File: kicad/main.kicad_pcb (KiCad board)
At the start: 2 copper layers, 13 parts, among them J1 Conn_02x14_Counter_Clockwise, U1 7421, U2 74LS86, U3 74LS138, U4 7421, U5 7421, U6 74LS138

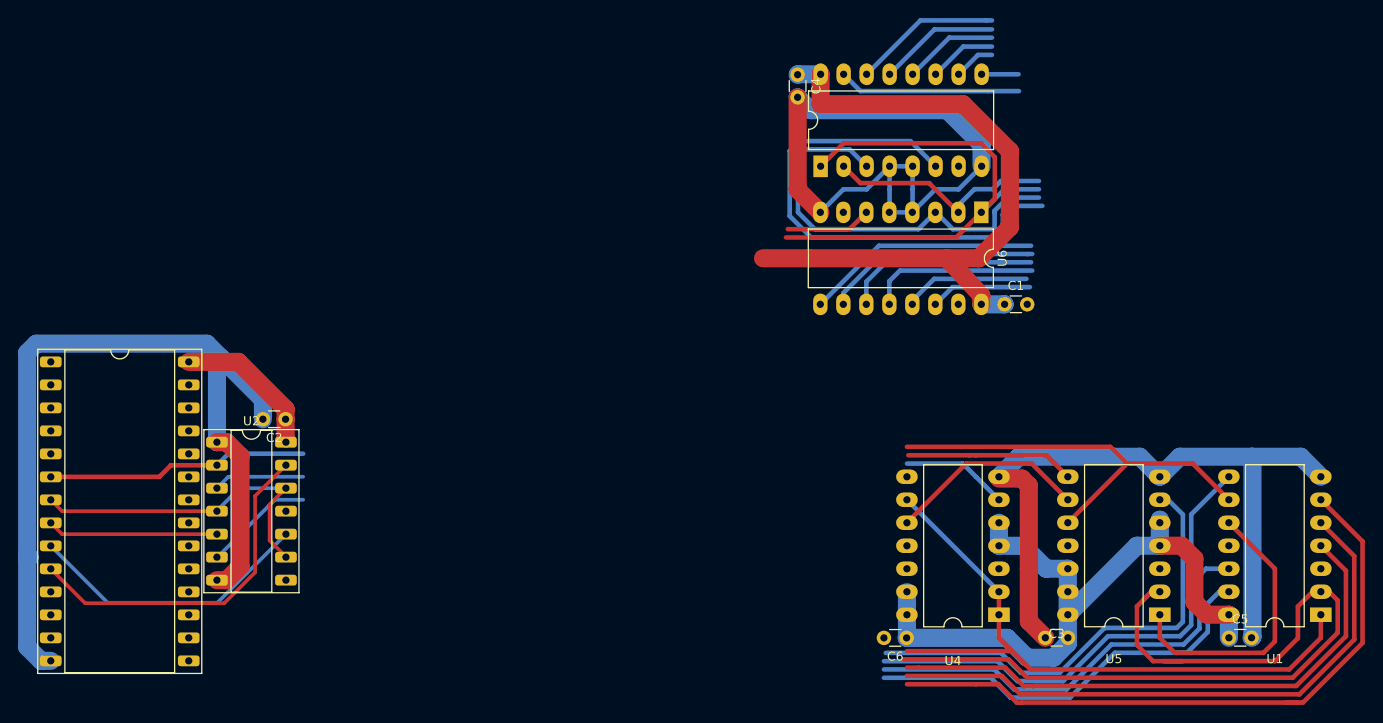
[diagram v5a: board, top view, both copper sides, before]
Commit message: finished single dmux
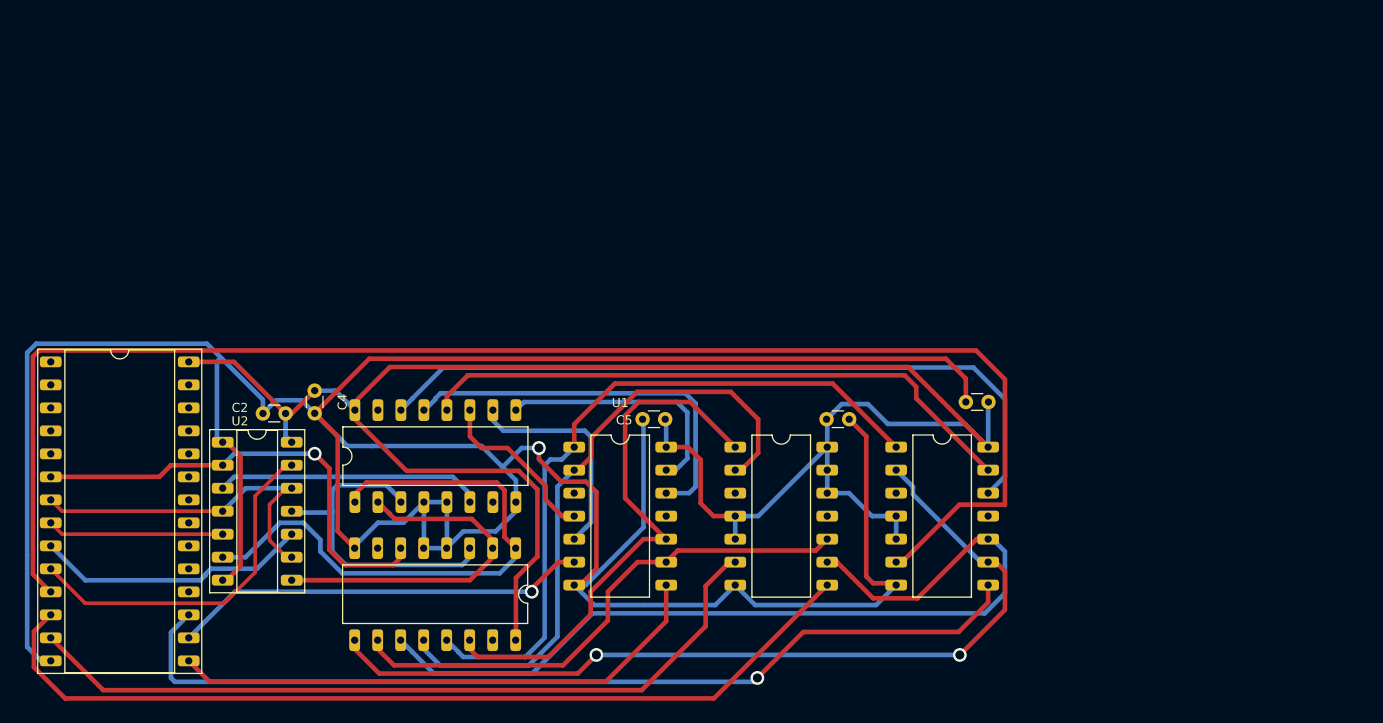
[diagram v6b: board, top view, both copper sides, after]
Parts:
- removed C1: 100n, Capacitor_THT:C_Disc_D3.0mm_W1.6mm_P2.50mm
- moved U1 84.5 mm to (108.0, 71.7), turned to 0 degrees
- moved C5 66.8 mm to (118.1, 68.6), turned to 180 degrees
- moved C4 63.7 mm to (79.4, 65.4)
- moved U3 63.4 mm to (83.8, 77.7)
- moved U6 63.4 mm to (101.6, 82.8)
- moved U5 50.4 mm to (125.8, 71.7), turned to 0 degrees
- moved C3 36.0 mm to (135.9, 68.6), turned to 0 degrees
- moved C6 27.6 mm to (153.8, 66.7)
- moved U4 21.7 mm to (143.6, 71.7), turned to 0 degrees
- moved U2 0.64 mm to (69.2, 71.1)
- moved C2 0.64 mm to (76.2, 67.9)
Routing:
- net /B_H_OUT: track 11.8 -> 164.2 mm
- net GND: track 249.3 -> 367.8 mm, vias 0 -> 1
- net /Y_L_OUT: track 0.00 -> 103.8 mm, vias 0 -> 1
- net /G_H_OUT: track 18.6 -> 100.8 mm
- net Net-(U3-~{Y1}): track 16.3 -> 81.3 mm
- net Net-(U6-~{Y6}): track 40.3 -> 98.2 mm, vias 0 -> 2
- net Net-(U6-~{Y4}): track 43.7 -> 101.1 mm
- net Net-(U3-~{Y3}): track 10.4 -> 67.3 mm
- net Net-(U3-~{Y4}): track 70.2 -> 19.0 mm
- net +5V: track 170.0 -> 220.8 mm
- net Net-(U3-~{Y5}): track 71.8 -> 24.8 mm
- net Net-(U6-~{Y3}): track 112.7 -> 71.3 mm
- net /adressInverter//PWM: track 66.5 -> 29.5 mm
- net /Y_H_OUT: track 51.2 -> 86.5 mm
- net /G_L_OUT: track 72.9 -> 46.2 mm, vias 0 -> 1
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
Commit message: final design
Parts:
- moved U6 2.18 mm to (101.6, 80.6)
- moved U3 1.53 mm to (83.8, 76.2)
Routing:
- net GND: track 367.8 -> 351.2 mm
- net /adressInverter/H1_OUT: track 64.0 -> 54.3 mm
- net Net-(U6-~{Y2}): track 78.5 -> 73.1 mm
- net /adressInverter/H2_OUT: track 40.4 -> 44.1 mm
- net /adressInverter/H3_OUT: track 37.4 -> 40.5 mm
- net Net-(U6-~{Y5}): track 59.0 -> 56.1 mm
- net Net-(U3-~{Y2}): track 44.0 -> 46.6 mm
- net Net-(U3-~{Y6}): track 27.7 -> 30.3 mm
- net Net-(U6-~{Y1}): track 60.4 -> 57.9 mm
- net Net-(U3-~{Y4}): track 19.0 -> 21.0 mm
- net Net-(U6-~{Y3}): track 71.3 -> 69.5 mm
- net /PWM_IN: track 51.2 -> 53.0 mm
- net /B_L_OUT: track 60.5 -> 58.7 mm
- net /G_H_OUT: track 100.8 -> 99.2 mm
- net /Y_H_OUT: track 86.5 -> 84.8 mm
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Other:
- board outline added: 109.5 x 38 mm
